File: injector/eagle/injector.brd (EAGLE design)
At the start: 34 x 35.8 mm, 34 parts, among them J4 ICSP, U1 ATA6631, U2 ATMEGA328, U3 ATA6631, X1 16MHz

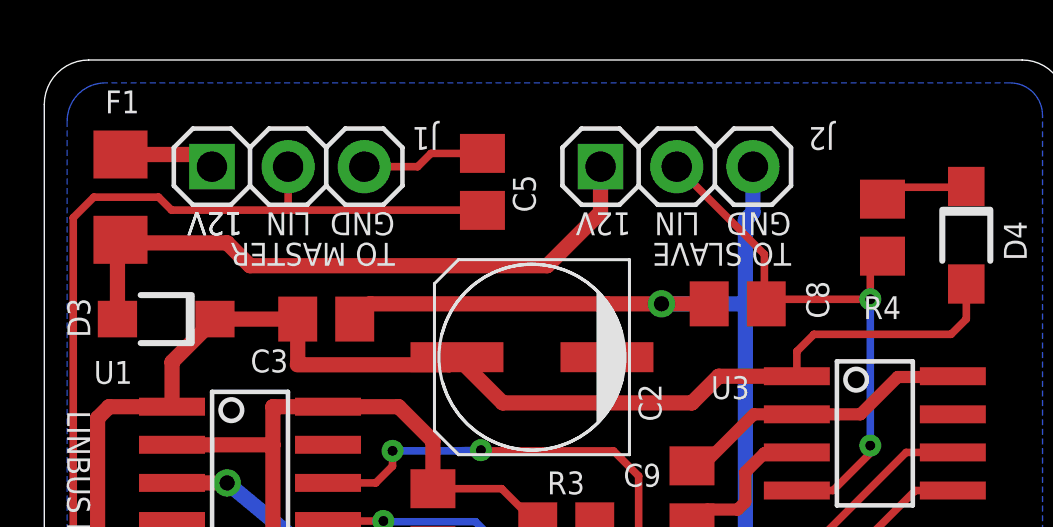
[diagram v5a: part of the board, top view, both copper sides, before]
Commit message: Moved J2 away from the big cap.
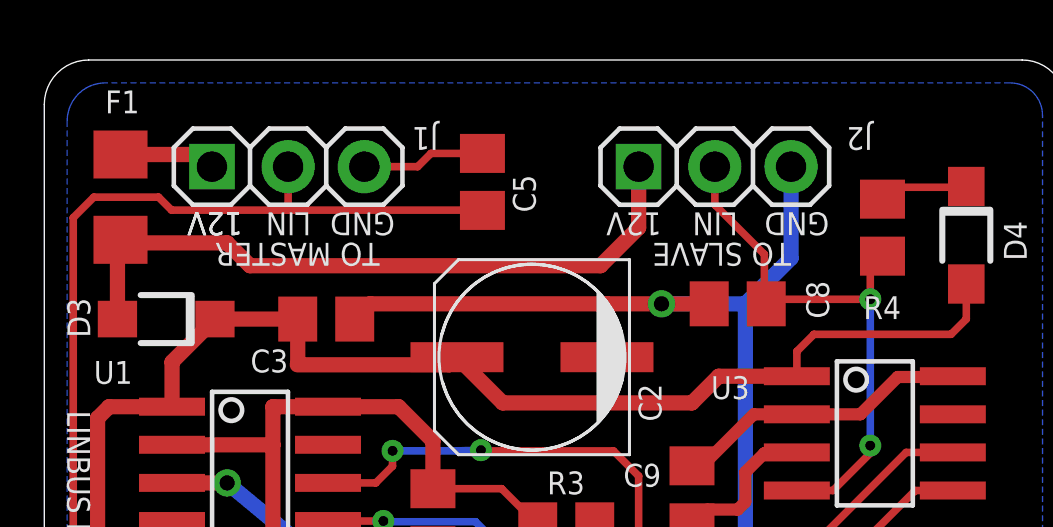
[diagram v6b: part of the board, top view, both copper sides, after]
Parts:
- moved J2 1.27 mm to (22.4, 32.3)
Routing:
- net N$6: track 21.3 -> 22.9 mm
- net LIN2: track 19.0 -> 18.5 mm
- net GND: track 98.1 -> 98.6 mm
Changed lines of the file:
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@@
 <text x="11.684" y="30.734" size="0.762" layer="21" rot="SR180">GND</text>
 <text x="6.604" y="30.734" size="0.762" layer="21" rot="SR180">12V</text>
-<text x="19.558" y="30.734" size="0.762" layer="21" rot="SR180">12V</text>
-<text x="21.844" y="30.734" size="0.762" layer="21" rot="SR180">LIN</text>
-<text x="24.892" y="30.734" size="0.762" layer="21" rot="SR180">GND</text>
+<text x="20.574" y="30.734" size="0.762" layer="21" rot="SR180">12V</text>
+<text x="23.114" y="30.734" size="0.762" layer="21" rot="SR180">LIN</text>
+<text x="26.162" y="30.734" size="0.762" layer="21" rot="SR180">GND</text>
 <text x="24.892" y="29.718" size="0.762" layer="21" rot="SR180">TO SLAVE</text>
-<text x="11.684" y="29.718" size="0.762" layer="21" rot="SR180">TO MASTER</text>
+<text x="11.176" y="29.718" size="0.762" layer="21" rot="SR180">TO MASTER</text>
 <text x="26.416" y="14.732" size="0.762" layer="21" rot="SR90">ICSP</text>
 <wire x1="26.162" y1="18.796" x2="26.162" y2="18.542" width="0.2032" layer="21"/>
@@
 <attribute name="VALUE" x="25.781" y="19.431" size="1.27" layer="27"/>
 </element>
-<element name="J2" library="injector" package="1X03" value="" x="21.082" y="32.258" smashed="yes">
-<attribute name="NAME" x="26.3398" y="33.5788" size="0.762" layer="25" ratio="10" rot="SR180"/>
-<attribute name="VALUE" x="17.272" y="29.083" size="1.27" layer="27"/>
+<element name="J2" library="injector" package="1X03" value="" x="22.352" y="32.258" smashed="yes">
+<attribute name="NAME" x="27.6098" y="33.5788" size="0.762" layer="25" ratio="10" rot="SR180"/>
+<attribute name="VALUE" x="18.542" y="29.083" size="1.27" layer="27"/>
 </element>
 <element name="C9" library="injector" package="C0805" value="0.1uF" x="21.59" y="21.336" smashed="yes" rot="R270">
@@
 <wire x1="12.888" y1="32.7" x2="12.446" y2="32.258" width="0.254" layer="1"/>
 <wire x1="12.446" y1="32.258" x2="10.668" y2="32.258" width="0.254" layer="1"/>
-<wire x1="23.368" y1="30.48" x2="23.622" y2="30.734" width="0.508" layer="16"/>
-<wire x1="23.622" y1="30.734" x2="23.622" y2="32.258" width="0.508" layer="16"/>
 <wire x1="18.756" y1="27.686" x2="20.574" y2="27.686" width="0.508" layer="1"/>
 <wire x1="20.574" y1="27.686" x2="22.164" y2="27.686" width="0.508" layer="1"/>
-<wire x1="23.368" y1="30.48" x2="23.368" y2="27.686" width="0.508" layer="16"/>
 <wire x1="23.368" y1="27.686" x2="20.574" y2="27.686" width="0.508" layer="16"/>
 <via x="20.574" y="27.686" extent="1-16" drill="0.508"/>
@@
 <wire x1="17.526" y1="13.208" x2="21.59" y2="13.208" width="0.254" layer="16"/>
 <wire x1="21.59" y1="13.208" x2="21.717" y2="13.335" width="0.254" layer="16"/>
+<wire x1="24.892" y1="32.258" x2="24.892" y2="29.21" width="0.508" layer="16"/>
+<wire x1="24.892" y1="29.21" x2="23.368" y2="27.686" width="0.508" layer="16"/>
 </signal>
 <signal name="N$3">
@@
 <wire x1="27.94" y1="29.2608" x2="27.94" y2="29.276" width="0.254" layer="1"/>
 <wire x1="27.5336" y1="27.8384" x2="27.5336" y2="22.9616" width="0.254" layer="16"/>
-<wire x1="24.003" y1="29.337" x2="21.082" y2="32.258" width="0.254" layer="1"/>
 <wire x1="24.003" y1="27.7876" x2="24.003" y2="29.337" width="0.254" layer="1"/>
 <wire x1="24.003" y1="27.7876" x2="24.064" y2="27.686" width="0.254" layer="1"/>
@@
 <wire x1="26.289" y1="21.463" x2="27.5336" y2="22.7076" width="0.254" layer="1"/>
 <wire x1="27.5336" y1="22.7076" x2="27.5336" y2="22.9616" width="0.254" layer="1"/>
+<wire x1="24.003" y1="29.337" x2="22.352" y2="30.988" width="0.254" layer="1"/>
+<wire x1="22.352" y1="30.988" x2="22.352" y2="32.258" width="0.254" layer="1"/>
 </signal>
 <signal name="N$6">
@@
 <wire x1="2.642" y1="29.718" x2="6.096" y2="29.718" width="0.508" layer="1"/>
 <wire x1="6.096" y1="29.718" x2="6.858" y2="28.956" width="0.508" layer="1"/>
-<wire x1="6.858" y1="28.956" x2="16.764" y2="28.956" width="0.508" layer="1"/>
-<wire x1="16.764" y1="28.956" x2="18.542" y2="30.734" width="0.508" layer="1"/>
-<wire x1="18.542" y1="30.734" x2="18.542" y2="32.258" width="0.508" layer="1"/>
+<wire x1="6.858" y1="28.956" x2="18.542" y2="28.956" width="0.508" layer="1"/>
+<wire x1="18.542" y1="28.956" x2="19.812" y2="30.226" width="0.508" layer="1"/>
+<wire x1="19.812" y1="30.226" x2="19.812" y2="32.258" width="0.508" layer="1"/>
 </signal>
 <signal name="LIN1_TX">

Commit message: Tweaked schema's annotations, updated layout PDF.
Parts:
- C3: value 0.1uF 40V -> 0.1uF 50V
- D5: value (none) -> RED
- D6, D7: value (none) -> GREEN
- D8: value (none) -> BLUE
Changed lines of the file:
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@@
 <attribute name="VALUE" x="23.495" y="7.874" size="1.27" layer="27" rot="R180"/>
 </element>
-<element name="C3" library="injector" package="C0805" value="0.1uF 40V" x="9.398" y="27.178" smashed="yes">
+<element name="C3" library="injector" package="C0805" value="0.1uF 50V" x="9.398" y="27.178" smashed="yes">
 <attribute name="NAME" x="8.128" y="26.162" size="0.762" layer="25" rot="R180"/>
 <attribute name="VALUE" x="8.128" y="24.638" size="1.27" layer="27"/>
@@
 <attribute name="VALUE" x="16.764" y="17.78" size="1.27" layer="27"/>
 </element>
-<element name="D5" library="injector" package="1206-LED" value="" x="29.972" y="7.874" smashed="yes">
+<element name="D5" library="injector" package="1206-LED" value="RED" x="29.972" y="7.874" smashed="yes">
 <attribute name="NAME" x="27.178" y="7.112" size="0.762" layer="25" rot="R90"/>
 <attribute name="VALUE" x="28.702" y="5.334" size="1.27" layer="27"/>
 </element>
-<element name="D6" library="injector" package="1206-LED" value="" x="29.972" y="5.334" smashed="yes">
+<element name="D6" library="injector" package="1206-LED" value="GREEN" x="29.972" y="5.334" smashed="yes">
 <attribute name="NAME" x="27.178" y="4.572" size="0.762" layer="25" rot="R90"/>
 <attribute name="VALUE" x="28.702" y="2.794" size="1.27" layer="27"/>
@@
 <attribute name="VALUE" x="2.707" y="18.002" size="1.27" layer="27" rot="R270"/>
 </element>
-<element name="D7" library="injector" package="1206-LED" value="" x="29.972" y="2.794" smashed="yes">
+<element name="D7" library="injector" package="1206-LED" value="GREEN" x="29.972" y="2.794" smashed="yes">
 <attribute name="NAME" x="27.178" y="2.032" size="0.762" layer="25" rot="R90"/>
 <attribute name="VALUE" x="28.702" y="0.254" size="1.27" layer="27"/>
 </element>
-<element name="D8" library="injector" package="1206-LED" value="" x="3.302" y="10.414" smashed="yes" rot="R90">
+<element name="D8" library="injector" package="1206-LED" value="BLUE" x="3.302" y="10.414" smashed="yes" rot="R90">
 <attribute name="NAME" x="2.1336" y="8.2804" size="0.762" layer="25" rot="R90"/>
 <attribute name="VALUE" x="5.842" y="9.144" size="1.27" layer="27" rot="R90"/>

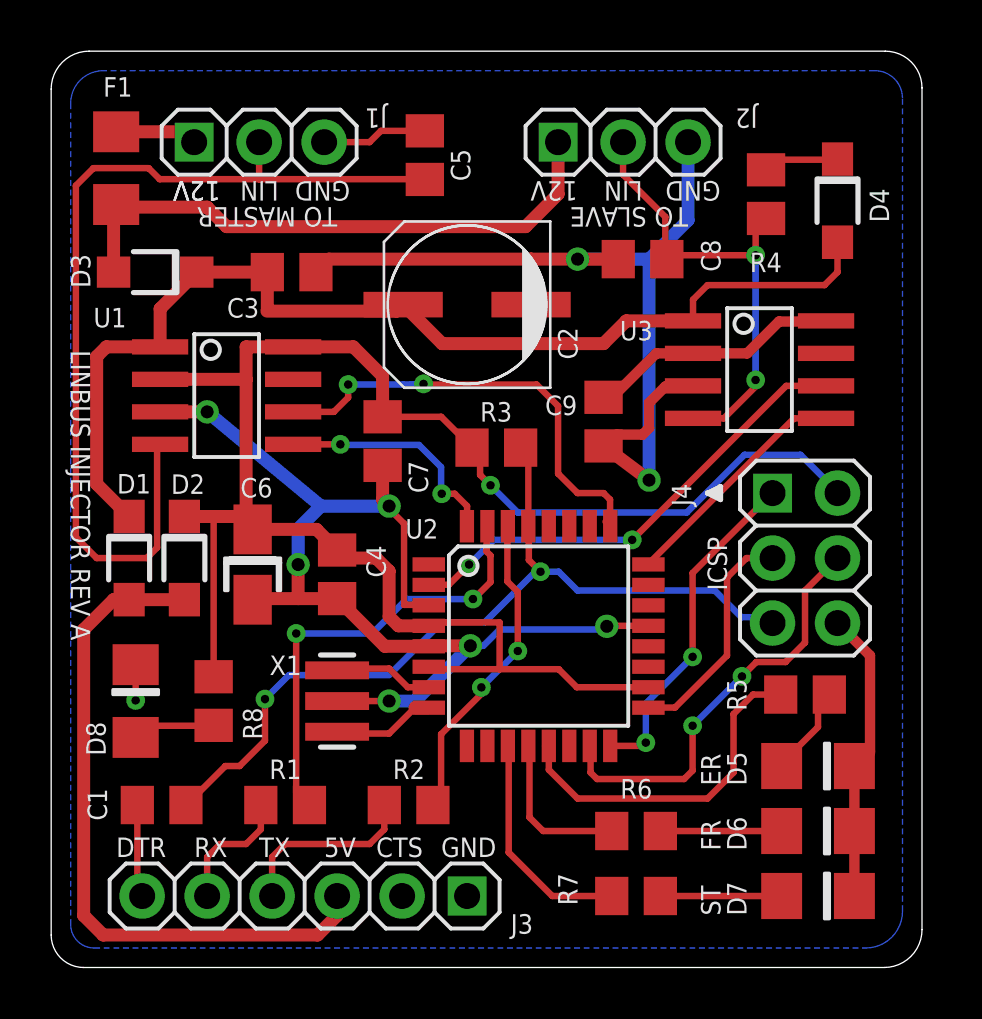
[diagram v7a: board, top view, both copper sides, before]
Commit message: Swapped the LIN and GND pins in the two 3 pin linbus headers. This will make this board consistent with the Beeper and Analyzer boards and with the P981 wiring.
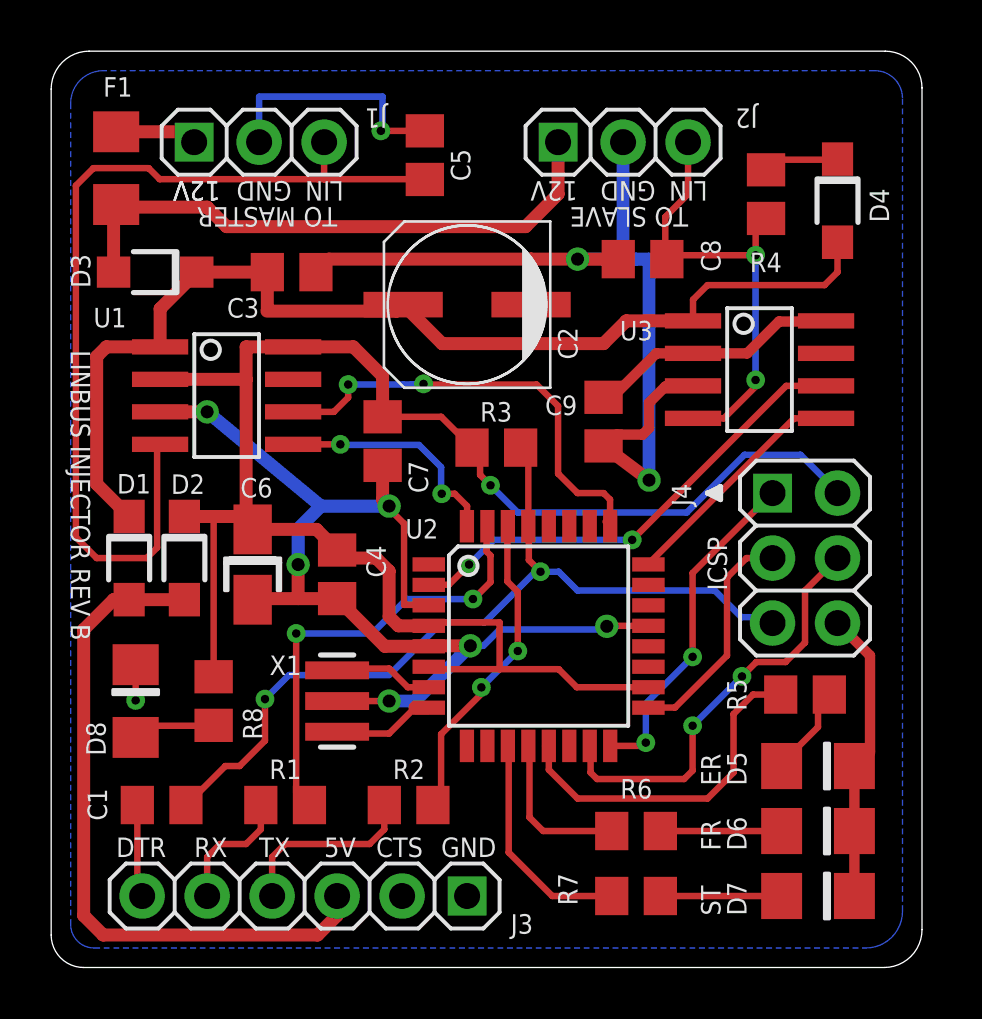
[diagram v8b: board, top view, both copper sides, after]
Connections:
- net GND: now also J1.2, J2.2; no longer J1.3, J2.3
- net LIN1: now also J1.3; no longer J1.2
- net LIN2: now also J2.3; no longer J2.2
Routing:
- net GND: track 98.6 -> 103.6 mm, vias 9 -> 10
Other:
- board text added: "LINBUS INJECTOR - REV B"
- board text added: "LINBUS INJECTOR REV B"
- board text removed: "LINBUS INJECTOR - REV A"
- board text removed: "LINBUS INJECTOR REV A"
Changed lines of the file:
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@@
 <rectangle x1="8.382" y1="23.368" x2="10.414" y2="23.876" layer="41"/>
 <text x="6.604" y="30.734" size="0.762" layer="21" rot="SR180">12V</text>
-<text x="8.89" y="30.734" size="0.762" layer="21" rot="SR180">LIN</text>
-<text x="11.684" y="30.734" size="0.762" layer="21" rot="SR180">GND</text>
+<text x="11.43" y="30.734" size="0.762" layer="21" rot="SR180">LIN</text>
+<text x="9.398" y="30.734" size="0.762" layer="21" rot="SR180">GND</text>
 <text x="6.604" y="30.734" size="0.762" layer="21" rot="SR180">12V</text>
 <text x="20.574" y="30.734" size="0.762" layer="21" rot="SR180">12V</text>
-<text x="23.114" y="30.734" size="0.762" layer="21" rot="SR180">LIN</text>
-<text x="26.162" y="30.734" size="0.762" layer="21" rot="SR180">GND</text>
+<text x="25.654" y="30.734" size="0.762" layer="21" rot="SR180">LIN</text>
+<text x="23.622" y="30.734" size="0.762" layer="21" rot="SR180">GND</text>
 <text x="24.892" y="29.718" size="0.762" layer="21" rot="SR180">TO SLAVE</text>
 <text x="11.176" y="29.718" size="0.762" layer="21" rot="SR180">TO MASTER</text>
@@
 <text x="5.588" y="4.318" size="0.762" layer="21" rot="SR0">RX</text>
 <text x="2.54" y="4.318" size="0.762" layer="21" rot="SR0">DTR</text>
-<text x="0.762" y="24.13" size="0.762" layer="21" rot="SR270">LINBUS INJECTOR REV A</text>
-<text x="1.016" y="28.321" size="1.016" layer="30" font="vector" ratio="15" rot="SMR90" align="bottom-right">LINBUS INJECTOR - REV A</text>
+<text x="0.762" y="24.13" size="0.762" layer="21" rot="SR270">LINBUS INJECTOR REV B</text>
+<text x="1.016" y="28.321" size="1.016" layer="30" font="vector" ratio="15" rot="SMR90" align="bottom-right">LINBUS INJECTOR - REV B</text>
 <text x="26.162" y="7.112" size="0.762" layer="21" rot="SR90">ER</text>
 <text x="26.162" y="4.572" size="0.762" layer="21" rot="SR90">FR</text>
@@
 <signals>
 <signal name="GND">
-<contactref element="J1" pad="3"/>
 <contactref element="C3" pad="2"/>
 <contactref element="C2" pad="-"/>
@@
 <contactref element="C6" pad="-"/>
 <contactref element="U1" pad="3"/>
-<contactref element="J2" pad="3"/>
 <contactref element="U3" pad="3"/>
 <contactref element="C9" pad="2"/>
@@
 <wire x1="9.652" y1="15.748" x2="9.652" y2="14.417" width="0.508" layer="1"/>
 <wire x1="14.605" y1="32.7" x2="12.888" y2="32.7" width="0.254" layer="1"/>
-<wire x1="12.888" y1="32.7" x2="12.446" y2="32.258" width="0.254" layer="1"/>
-<wire x1="12.446" y1="32.258" x2="10.668" y2="32.258" width="0.254" layer="1"/>
 <wire x1="18.756" y1="27.686" x2="20.574" y2="27.686" width="0.508" layer="1"/>
 <wire x1="20.574" y1="27.686" x2="22.164" y2="27.686" width="0.508" layer="1"/>
-<wire x1="23.368" y1="27.686" x2="20.574" y2="27.686" width="0.508" layer="16"/>
+<wire x1="23.368" y1="27.686" x2="22.86" y2="27.686" width="0.508" layer="16"/>
 <via x="20.574" y="27.686" extent="1-16" drill="0.508"/>
+<wire x1="22.352" y1="27.686" x2="20.574" y2="27.686" width="0.508" layer="16"/>
 <wire x1="13.7922" y1="14.1732" x2="14.7574" y2="14.1732" width="0.254" layer="1"/>
 <wire x1="13.7922" y1="17.3482" x2="13.7922" y2="14.1732" width="0.254" layer="1"/>
@@
 <wire x1="17.526" y1="13.208" x2="21.59" y2="13.208" width="0.254" layer="16"/>
 <wire x1="21.59" y1="13.208" x2="21.717" y2="13.335" width="0.254" layer="16"/>
-<wire x1="24.892" y1="32.258" x2="24.892" y2="29.21" width="0.508" layer="16"/>
-<wire x1="24.892" y1="29.21" x2="23.368" y2="27.686" width="0.508" layer="16"/>
+<contactref element="J1" pad="2"/>
+<contactref element="J2" pad="2"/>
+<via x="12.888" y="32.7" extent="1-16" drill="0.3302"/>
+<wire x1="12.888" y1="32.7" x2="12.954" y2="32.7" width="0.254" layer="16"/>
+<wire x1="12.954" y1="32.7" x2="12.954" y2="34.036" width="0.254" layer="16"/>
+<wire x1="12.954" y1="34.036" x2="8.128" y2="34.036" width="0.254" layer="16"/>
+<wire x1="8.128" y1="34.036" x2="8.128" y2="32.258" width="0.254" layer="16"/>
+<wire x1="22.352" y1="32.258" x2="22.352" y2="27.686" width="0.508" layer="16"/>
+<wire x1="22.352" y1="27.686" x2="22.86" y2="27.686" width="0.508" layer="16"/>
 </signal>
 <signal name="N$3">
@@
 </signal>
 <signal name="LIN1">
-<contactref element="J1" pad="2"/>
 <contactref element="U1" pad="4"/>
 <contactref element="C5" pad="1"/>
-<wire x1="8.128" y1="30.8102" x2="14.605" y2="30.8102" width="0.254" layer="1"/>
-<wire x1="8.128" y1="32.258" x2="8.128" y2="30.8102" width="0.254" layer="1"/>
+<wire x1="10.668" y1="30.8102" x2="14.605" y2="30.8102" width="0.254" layer="1"/>
 <wire x1="14.605" y1="30.8102" x2="14.605" y2="30.8" width="0.254" layer="1"/>
 <wire x1="4.2418" y1="20.447" x2="4.258" y2="20.447" width="0.254" layer="1"/>
@@
 <wire x1="1.651" y1="31.242" x2="3.81" y2="31.242" width="0.254" layer="1"/>
 <wire x1="3.81" y1="31.242" x2="4.2418" y2="30.8102" width="0.254" layer="1"/>
-<wire x1="4.2418" y1="30.8102" x2="8.128" y2="30.8102" width="0.254" layer="1"/>
+<wire x1="4.2418" y1="30.8102" x2="10.414" y2="30.8102" width="0.254" layer="1"/>
 <wire x1="4.1402" y1="20.2184" x2="4.258" y2="20.3362" width="0.254" layer="1"/>
 <wire x1="4.258" y1="20.3362" x2="4.258" y2="20.447" width="0.254" layer="1"/>
+<contactref element="J1" pad="3"/>
+<wire x1="10.668" y1="32.258" x2="10.668" y2="30.8102" width="0.254" layer="1"/>
+<wire x1="10.668" y1="30.8102" x2="10.414" y2="30.8102" width="0.254" layer="1"/>
 </signal>
 <signal name="+12V">
@@
 </signal>
 <signal name="LIN2">
-<contactref element="J2" pad="2"/>
 <contactref element="R4" pad="2"/>
 <contactref element="C8" pad="1"/>
@@
 <wire x1="26.289" y1="21.463" x2="27.5336" y2="22.7076" width="0.254" layer="1"/>
 <wire x1="27.5336" y1="22.7076" x2="27.5336" y2="22.9616" width="0.254" layer="1"/>
-<wire x1="24.003" y1="29.337" x2="22.352" y2="30.988" width="0.254" layer="1"/>
-<wire x1="22.352" y1="30.988" x2="22.352" y2="32.258" width="0.254" layer="1"/>
+<contactref element="J2" pad="3"/>
+<wire x1="24.003" y1="29.337" x2="24.892" y2="30.226" width="0.254" layer="1"/>
+<wire x1="24.892" y1="30.226" x2="24.892" y2="32.258" width="0.254" layer="1"/>
 </signal>
 <signal name="N$6">
